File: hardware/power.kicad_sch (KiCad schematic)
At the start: 3 parts, among them U2 TPS54360DDA, U3 NCP1117-3.3_SOT223

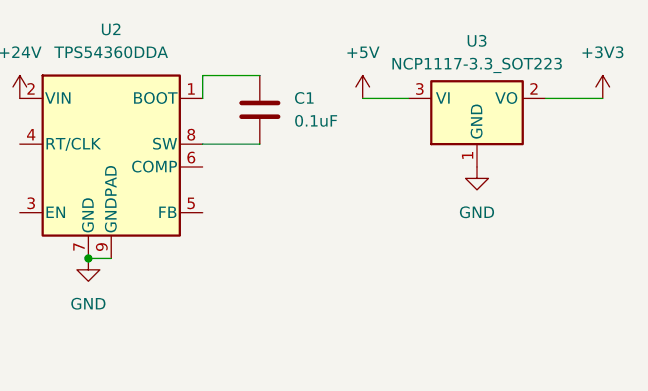
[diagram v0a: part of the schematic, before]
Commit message: Add JLCPCB assembly path for the buck
The Recom module is SIP-3 through-hole and unlikely to be in JLC's library.
Documents two routes: mark it DNP and hand-solder three pins after assembly,
which keeps the 72 V margin and one-part simplicity; or switch to an SMD part
JLC stocks.

Lists selection criteria and three candidates to check against the live parts
library - LM2675MX-5.0 (best if stocked), XL1509-5.0E1 (cheap, near-certain
LCSC stock, but 150 kHz means a bulky inductor), and MP4560 (55 V, better
margin). Notes that stock cannot be verified from here.
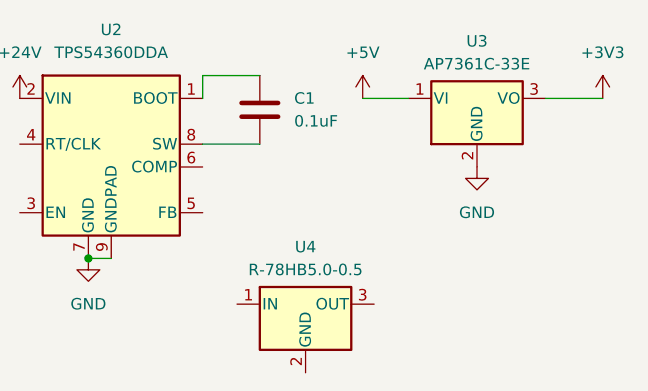
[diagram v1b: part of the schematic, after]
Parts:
- removed U3: NCP1117-3.3_SOT223, Package_TO_SOT_SMD:SOT-223-3_TabPin2, symbol Regulator_Linear:NCP1117-3.3_SOT223
- added U3: AP7361C-33E, Package_TO_SOT_SMD:SOT-223-3_TabPin2, symbol Regulator_Linear:AP7361C-33E
- added U4: R-78HB5.0-0.5, Converter_DCDC:Converter_DCDC_RECOM_R-78HB-0.5_THT, symbol Converter_DCDC:R-78HB5.0-0.5
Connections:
- net +3V3: now also U3.3 (VO)
- net +5V: now also U3.1 (VI)
- net GND: now also U3.2 (GND)
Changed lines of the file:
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@@
 	)
 	(symbol
-		(lib_id "Regulator_Linear:NCP1117-3.3_SOT223")
+		(lib_id "Regulator_Linear:AP7361C-33E")
 		(at 137.16 54.61 0)
 		(unit 1)
@@
 			)
 		)
-		(property "Value" "NCP1117-3.3_SOT223"
+		(property "Value" "AP7361C-33E"
 			(at 137.16 50.8 0)
 			(show_name no)
@@
 		)
 		(property "Footprint" "Package_TO_SOT_SMD:SOT-223-3_TabPin2"
-			(at 137.16 49.53 0)
+			(at 137.16 48.895 0)
+			(hide yes)
+			(show_name no)
+			(do_not_autoplace no)
+			(effects
+				(font
+					(size 1.27 1.27)
+					(italic yes)
+				)
+			)
+		)
+		(property "Datasheet" "https://www.diodes.com/assets/Datasheets/AP7361C.pdf"
+			(at 137.16 55.88 0)
 			(hide yes)
 			(show_name no)
@@
 			)
 		)
-		(property "Datasheet" "http://www.onsemi.com/pub_link/Collateral/NCP1117-D.PDF"
-			(at 139.7 60.96 0)
-			(hide yes)
-			(show_name no)
-			(do_not_autoplace no)
-			(effects
-				(font
-					(size 1.27 1.27)
-				)
-			)
-		)
-		(property "Description" "1A Low drop-out regulator, Fixed Output 3.3V, SOT-223"
+		(property "Description" "1A Low Dropout regulator, positive, 3.3V fixed output, SOT-223"
 			(at 137.16 54.61 0)
 			(hide yes)
@@
 					(unit 1)
 				)
+			)
+		)
+	)
+	(symbol
+		(lib_id "Converter_DCDC:R-78HB5.0-0.5")
+		(at 118.11 77.47 0)
+		(unit 1)
+		(body_style 1)
+		(exclude_from_sim no)
+		(in_bom yes)
+		(on_board yes)
+		(in_pos_files yes)
+		(dnp no)
+		(fields_autoplaced yes)
+		(property "Reference" "U4"
+			(at 118.11 71.12 0)
+			(show_name no)
+			(do_not_autoplace no)
+			(effects
+				(font
+					(size 1.27 1.27)
+				)
+			)
+		)
+		(property "Value" "R-78HB5.0-0.5"
+			(at 118.11 73.66 0)
+			(show_name no)
+			(do_not_autoplace no)
+			(effects
+				(font
+					(size 1.27 1.27)
+				)
+			)
+		)
+		(property "Footprint" "Converter_DCDC:Converter_DCDC_RECOM_R-78HB-0.5_THT"
+			(at 119.38 83.82 0)
+			(hide yes)
+			(show_name no)
+			(do_not_autoplace no)
+			(effects
+				(font
+					(size 1.27 1.27)
+					(italic yes)
+				)
+				(justify left)
+			)
+		)
+		(property "Datasheet" "https://www.recom-power.com/pdf/Innoline/R-78HBxx-0.5_L.pdf"
+			(at 118.11 77.47 0)
+			(hide yes)
+			(show_name no)
+			(do_not_autoplace no)
+			(effects
+				(font
+					(size 1.27 1.27)
+				)
+			)
+		)
+		(property "Description" "500mA Step-Down DC/DC-Regulator, 9-72V input, 5.0V fixed Output Voltage, LM78xx replacement, -40°C to +85°C, SIP3"
+			(at 118.11 77.47 0)
+			(hide yes)
+			(show_name no)
+			(do_not_autoplace no)
+			(effects
+				(font
+					(size 1.27 1.27)
+				)
+			)
+		)
+		(pin "3"
+		)
+		(pin "2"
+		)
+		(pin "1"
+		)
+		(instances
+			(project "ufluidics"
+				(path "/bf8ba2d7-3b7b-4865-bab6-5f38b618ecb0/5a66379a-5c74-405f-af46-36bdd39f35a7"
+					(reference "U4")
+					(unit 1)
+				)

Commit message: make the schematics
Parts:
- removed U2: TPS54360DDA, Package_SO:TI_SO-PowerPAD-8_ThermalVias, symbol Regulator_Switching:TPS54360DDA
- removed U4: R-78HB5.0-0.5, Converter_DCDC:Converter_DCDC_RECOM_R-78HB-0.5_THT, symbol Converter_DCDC:R-78HB5.0-0.5
- added C8: 1uF, symbol Device:C
- added C9: 470uF, symbol Device:C
- added Cin1, Cin2, Cin3: 4.7uF, symbol Device:C
- added Cinx1: 100nF, symbol Device:C
- added Cout1, Cout2: 68uF, symbol Device:C
- added D2: B140-E3, Diode_SMD:D_SMA, symbol Diode:B140-E3
- added D6: SMBJ26A, Diode_SMD:D_SMB, symbol Diode:SM6T33A
- added D7: BZV55C15, Diode_SMD:D_MiniMELF, symbol Diode:BZV55C15
- added F1: 2 A, 5x20 mm, Fuse:Fuseholder_Cylinder-5x20mm_Stelvio-Kontek_PTF78_Horizontal_Open, symbol Device:Fuse
- added J18: Screw_Terminal_01x02, symbol Connector:Screw_Terminal_01x02
- added L1: 47uH, symbol Device:L
- added Q1: SUD50P06-15, Package_TO_SOT_SMD:TO-252-2, symbol Transistor_FET:SUD50P06-15
- added R11: 100k, symbol Device:R
- added U5: LM2675M-5, Package_SO:SOIC-8_3.9x4.9mm_P1.27mm, symbol Regulator_Switching:LM2675M-5
- C1: value 0.1uF -> 10nF
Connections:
- net +24V: now also C9.2, Cin1.2, Cin2.2, Cin3.2, Cinx1.2, D6.2 (A2), D7.1 (K), Q1.3 (S), U5.7 (VIN)
- net +3V3: now also C8.1
- net +5V: now also Cout1.2, Cout2.2, L1.2, U5.4 (FB)
- net GND: now also C8.2, C9.1, Cin1.1, Cin2.1, Cin3.1, Cinx1.1, Cout1.1, Cout2.1, D2.2 (A), D6.1 (A1), J18.1 (Pin_1), R11.2, U5.6 (GND)
- net at C1.1: now also U5.1 (CB)
- net at C1.2: now also D2.1 (K), L1.1, U5.8 (VSW)
- new net: D7.2 (A), Q1.1 (G), R11.1
- new net: F1.2, Q1.2 (D)
- new net: F1.1, J18.2 (Pin_2)
- no-connect marks 0 -> 1
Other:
- note added: "Buck-buck converter (24V -> 5V)"
- note added: "Cin and Cout must be tantalum Cin must have 50V Cout must have 25V"
- note added: "LDO (5V -> 3.3V)"
- note added: "Power input"
- moved on the sheet: U3

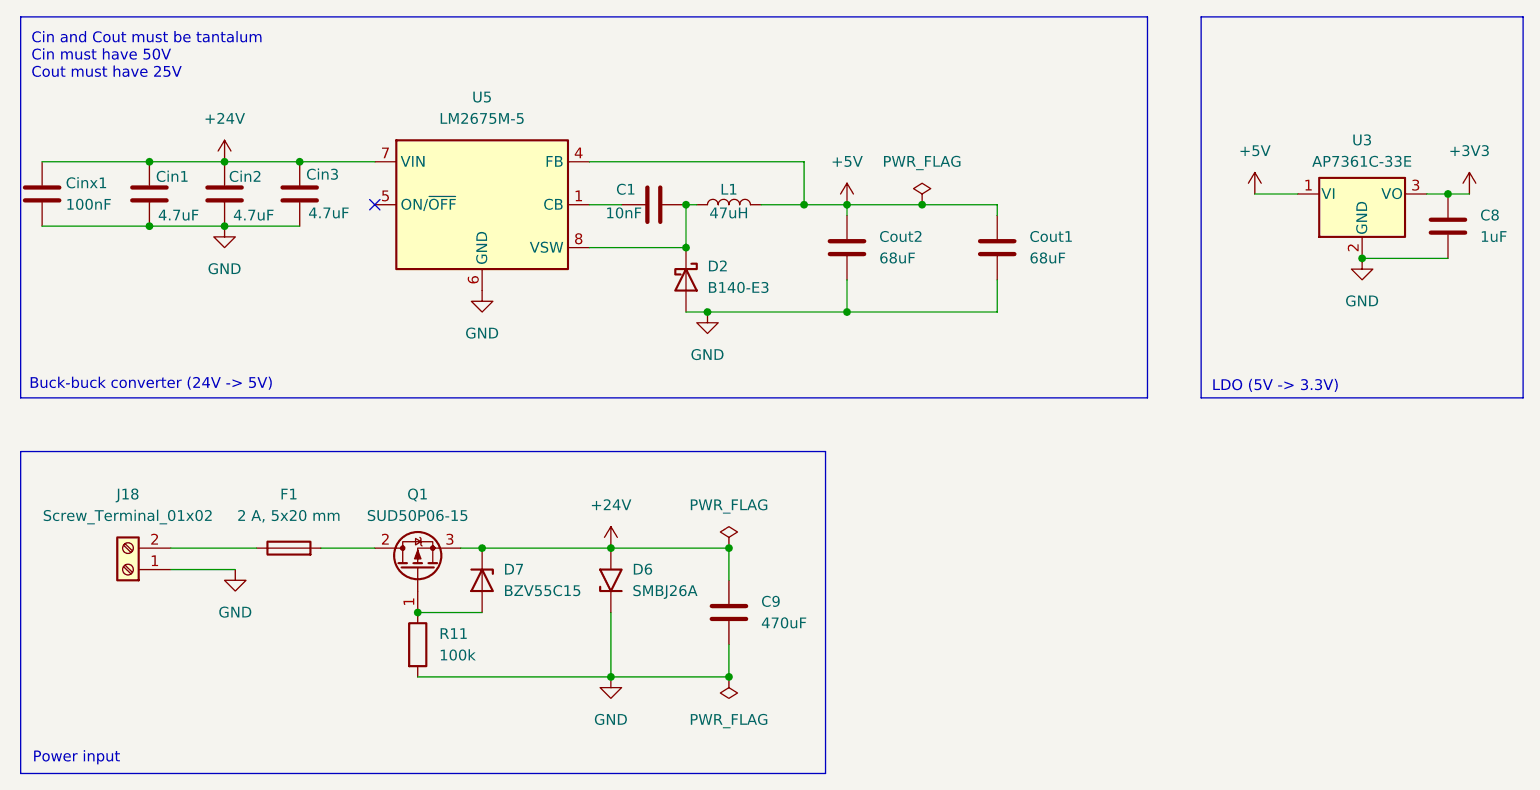
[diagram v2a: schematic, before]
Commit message: place the stuff on the pcb
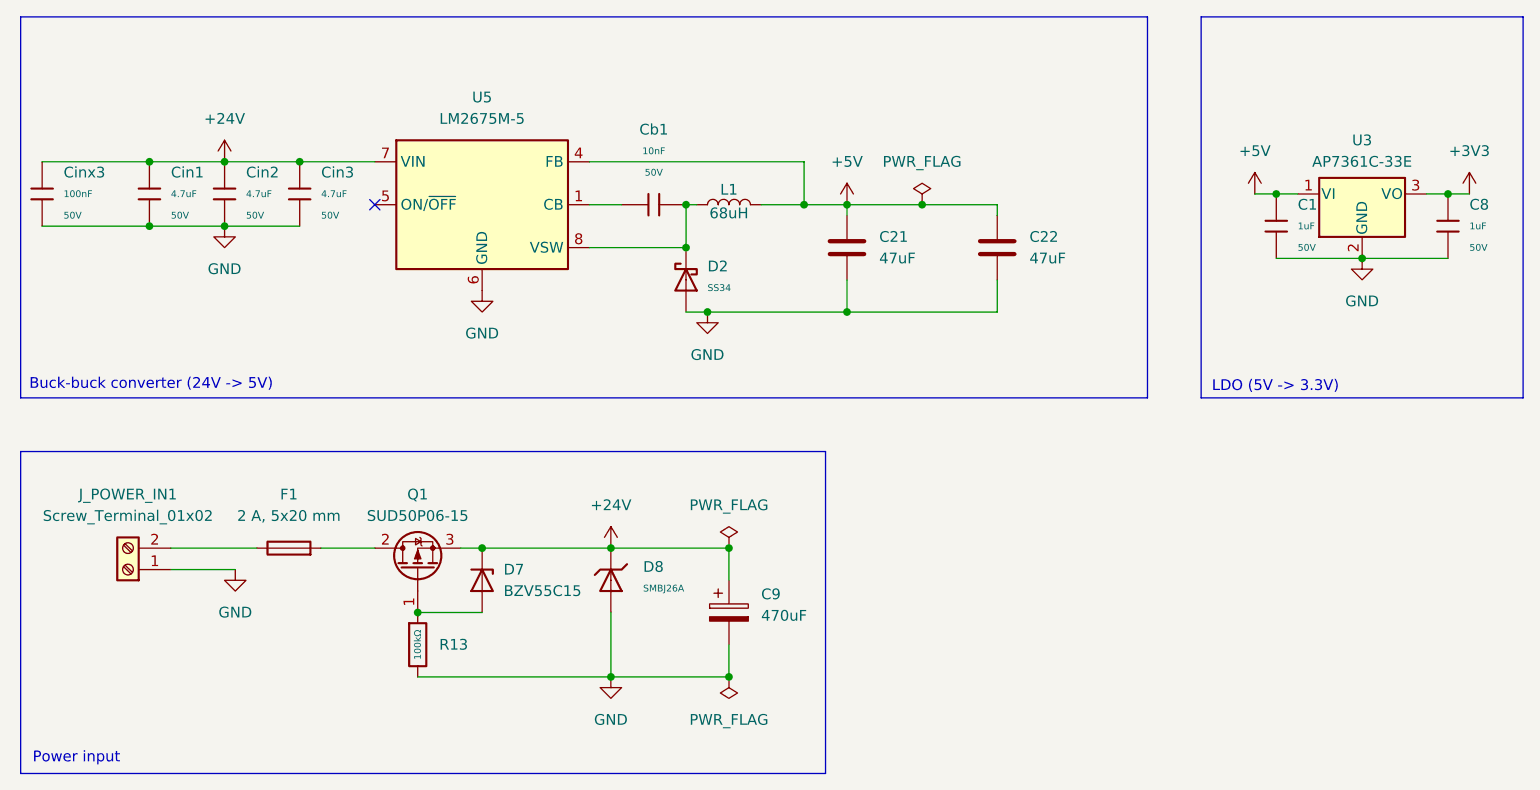
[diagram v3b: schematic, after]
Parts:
- removed C1: 10nF, symbol Device:C
- removed C8: 1uF, symbol Device:C
- removed C9: 470uF, symbol Device:C
- removed Cin1, Cin2, Cin3: 4.7uF, symbol Device:C
- removed Cinx1: 100nF, symbol Device:C
- removed Cout1, Cout2: 68uF, symbol Device:C
- removed D2: B140-E3, Diode_SMD:D_SMA, symbol Diode:B140-E3
- removed D6: SMBJ26A, Diode_SMD:D_SMB, symbol Diode:SM6T33A
- removed R11: 100k, symbol Device:R
- added C1, C8: 1uF, PCM_JLCPCB:C_0805, symbol PCM_JLCPCB-Capacitors:0805,1uF
- added C21, C22: 47uF, Capacitor_SMD:C_1210_3225Metric, symbol Device:C
- added C9: 470uF, Capacitor_Tantalum_SMD:CP_EIA-7343-31_Kemet-D, symbol Device:C_Polarized
- added Cb1: 10nF, PCM_JLCPCB:C_0805, symbol PCM_JLCPCB-Capacitors:0805,10nF
- added Cin1, Cin2, Cin3: 4.7uF, PCM_JLCPCB:C_1206, symbol PCM_JLCPCB-Capacitors:1206,4.7uF
- added Cinx3: 100nF, PCM_JLCPCB:C_0402, symbol PCM_JLCPCB-Capacitors:0402,100nF,(2)
- added D2: SS34, PCM_JLCPCB:D_SMA, symbol PCM_JLCPCB-Diodes:Schottky,SS34
- added D8: SMBJ26A, PCM_JLCPCB:D_SMB, symbol PCM_JLCPCB-Diodes:TVS-Uni,SMBJ26A
- added R13: 100kΩ, PCM_JLCPCB:R_0603, symbol PCM_JLCPCB-Resistors:0603,100kΩ
- F1: JLC Part# (none) -> C3130
- J_POWER_IN1: renamed from J18; footprint (none) -> TerminalBlock_4Ucon:TerminalBlock_4Ucon_1x02_P3.50mm_Horizontal
- L1: value 47uH -> 68uH; footprint (none) -> Inductor_SMD:L_SXN_SMDRI127; JLC Part# (none) -> C9907; MFR Part# (none) -> SMDRI127-680MT
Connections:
- net +24V: now also C9.1, Cin1.1, Cin2.1, Cin3.1, Cinx3.1, D8.1
- net +3V3: now also C8.1
- net +5V: now also C1.1, C21.1, C22.1
- net GND: now also C1.2, C21.2, C22.2, C8.2, C9.2, Cin1.2, Cin2.2, Cin3.2, Cinx3.2, D2.2, D8.2, R13.2
- net at U5.1 (CB): now also Cb1.1
- net at L1.1, U5.8 (VSW): now also Cb1.2, D2.1
- net at D7.2 (A), Q1.1 (G): now also R13.1
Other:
- note removed: "Cin and Cout must be tantalum Cin must have 50V Cout must have 25V"

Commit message: route
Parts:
- removed C9: 470uF, Capacitor_Tantalum_SMD:CP_EIA-7343-31_Kemet-D, symbol Device:C_Polarized
- added C5: 470 uF 35V, Capacitor_THT:C_Radial_D10.0mm_H16.0mm_P5.00mm, symbol Device:C
- added J18: Conn_01x03, Connector_PinHeader_2.54mm:PinHeader_1x03_P2.54mm_Vertical, symbol Connector_Generic:Conn_01x03
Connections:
- net +24V: now also C5.1
- net +3V3: now also J18.2 (Pin_2)
- net +5V: now also J18.1 (Pin_1)
- net GND: now also C5.2, J18.3 (Pin_3)
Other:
- note added: "Power Headers"
